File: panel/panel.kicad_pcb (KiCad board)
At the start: 2 copper layers, 199.5 x 80 mm, 381 parts, among them J1 Conn_01x02, J2 Conn_01x03, J3 Conn_01x05, J4 HRO-TYPE-C-31-M-12, J5 ICSP, SW1 SW_RESET, U1 CH340G, U2 ATmega328P-AU, U3 LM324DT, U4 LM324DT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

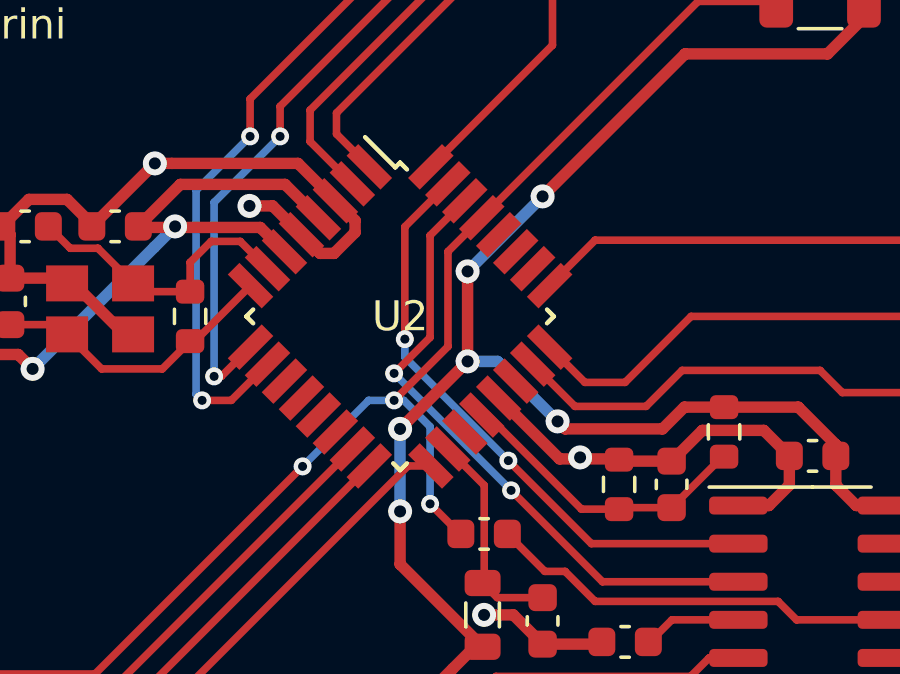
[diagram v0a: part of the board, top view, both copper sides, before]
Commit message: errata 1: rx and tx are flipped
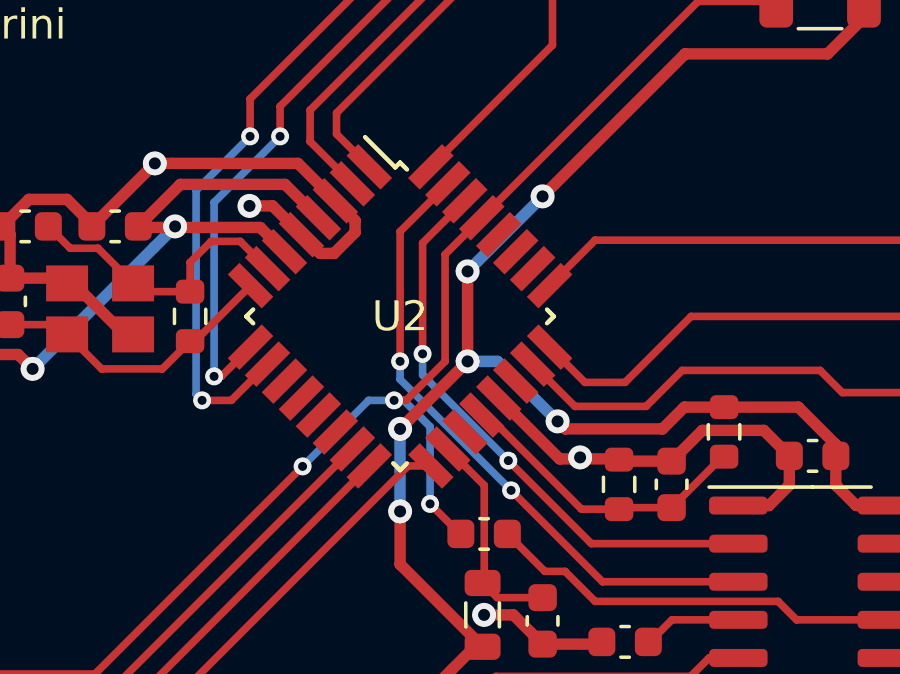
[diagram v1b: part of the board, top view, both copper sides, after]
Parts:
- removed the REF** at (239.0, 120.0) (x2)
- removed the REF** at (197.3, 120.6) (x2)
- removed the REF** at (61.7, 120.0) (x2)
- removed the REF** at (60.5, 118.9) (x2)
- removed the REF** at (61.1, 119.4) (x2)
- removed the REF** at (58.8, 117.1) (x2)
- removed the REF** at (59.4, 117.7) (x2)
- removed the REF** at (60.0, 118.3) (x2)
- removed the REF** at (60.0, 74.8) (x2)
- removed the REF** at (106.3, 117.7) (x2)
- removed the REF** at (193.8, 117.1) (x2)
- removed the REF** at (62.3, 72.5) (x2)
- removed the REF** at (59.4, 75.4) (x2)
- removed the REF** at (106.9, 117.1) (x2)
- removed the REF** at (61.7, 73.1) (x2)
- removed the REF** at (105.2, 118.9) (x2)
- removed the REF** at (105.7, 118.3) (x2)
- removed the REF** at (58.8, 76.0) (x2)
- removed the REF** at (61.1, 73.7) (x2)
- removed the REF** at (60.5, 74.2) (x2)
- removed the REF** at (103.4, 120.6) (x2)
- removed the REF** at (196.7, 120.0) (x2)
- removed the REF** at (104.6, 73.7) (x2)
- removed the REF** at (106.9, 76.0) (x2)
- removed the REF** at (106.3, 75.4) (x2)
- removed the REF** at (105.2, 74.2) (x2)
- removed the REF** at (103.4, 72.5) (x2)
- removed the REF** at (104.0, 73.1) (x2)
- removed the REF** at (105.7, 74.8) (x2)
- removed the REF** at (195.0, 118.3) (x2)
- removed the REF** at (194.4, 117.7) (x2)
- removed the REF** at (195.5, 118.9) (x2)
- removed the REF** at (196.1, 119.4) (x2)
- removed the REF** at (239.6, 119.4) (x2)
- removed the REF** at (195.0, 74.8) (x2)
- removed the REF** at (241.3, 117.7) (x2)
- removed the REF** at (197.3, 72.5) (x2)
- removed the REF** at (194.4, 75.4) (x2)
- removed the REF** at (241.9, 117.1) (x2)
- removed the REF** at (196.7, 73.1) (x2)
- removed the REF** at (238.4, 120.6) (x2)
- removed the REF** at (240.2, 118.9) (x2)
- removed the REF** at (240.7, 118.3) (x2)
- removed the REF** at (193.8, 76.0) (x2)
- removed the REF** at (196.1, 73.7) (x2)
- removed the REF** at (195.5, 74.2) (x2)
- removed the REF** at (239.6, 73.7) (x2)
- removed the REF** at (241.9, 76.0) (x2)
- removed the REF** at (241.3, 75.4) (x2)
- removed the REF** at (240.2, 74.2) (x2)
- removed the REF** at (238.4, 72.5) (x2)
- removed the REF** at (239.0, 73.1) (x2)
- removed the REF** at (240.7, 74.8) (x2)
- removed the REF** at (104.0, 120.0) (x2)
- removed the REF** at (104.6, 119.4) (x2)
- removed the REF** at (62.3, 120.6) (x2)
- added REF** (x2): NPTH, NPTH, F.Cu at (239.0, 120.0)
- added REF** (x2): NPTH, NPTH, F.Cu at (197.3, 120.6)
- added REF** (x2): NPTH, NPTH, F.Cu at (61.7, 120.0)
- added REF** (x2): NPTH, NPTH, F.Cu at (60.5, 118.9)
- added REF** (x2): NPTH, NPTH, F.Cu at (61.1, 119.4)
- added REF** (x2): NPTH, NPTH, F.Cu at (58.8, 117.1)
- added REF** (x2): NPTH, NPTH, F.Cu at (59.4, 117.7)
- added REF** (x2): NPTH, NPTH, F.Cu at (60.0, 118.3)
- added REF** (x2): NPTH, NPTH, F.Cu at (60.0, 74.8)
- added REF** (x2): NPTH, NPTH, F.Cu at (106.3, 117.7)
- added REF** (x2): NPTH, NPTH, F.Cu at (193.8, 117.1)
- added REF** (x2): NPTH, NPTH, F.Cu at (62.3, 72.5)
- added REF** (x2): NPTH, NPTH, F.Cu at (59.4, 75.4)
- added REF** (x2): NPTH, NPTH, F.Cu at (106.9, 117.1)
- added REF** (x2): NPTH, NPTH, F.Cu at (61.7, 73.1)
- added REF** (x2): NPTH, NPTH, F.Cu at (105.2, 118.9)
- added REF** (x2): NPTH, NPTH, F.Cu at (105.7, 118.3)
- added REF** (x2): NPTH, NPTH, F.Cu at (58.8, 76.0)
- added REF** (x2): NPTH, NPTH, F.Cu at (61.1, 73.7)
- added REF** (x2): NPTH, NPTH, F.Cu at (60.5, 74.2)
- added REF** (x2): NPTH, NPTH, F.Cu at (103.4, 120.6)
- added REF** (x2): NPTH, NPTH, F.Cu at (196.7, 120.0)
- added REF** (x2): NPTH, NPTH, F.Cu at (104.6, 73.7)
- added REF** (x2): NPTH, NPTH, F.Cu at (106.9, 76.0)
- added REF** (x2): NPTH, NPTH, F.Cu at (106.3, 75.4)
- added REF** (x2): NPTH, NPTH, F.Cu at (105.2, 74.2)
- added REF** (x2): NPTH, NPTH, F.Cu at (103.4, 72.5)
- added REF** (x2): NPTH, NPTH, F.Cu at (104.0, 73.1)
- added REF** (x2): NPTH, NPTH, F.Cu at (105.7, 74.8)
- added REF** (x2): NPTH, NPTH, F.Cu at (195.0, 118.3)
- added REF** (x2): NPTH, NPTH, F.Cu at (194.4, 117.7)
- added REF** (x2): NPTH, NPTH, F.Cu at (195.5, 118.9)
- added REF** (x2): NPTH, NPTH, F.Cu at (196.1, 119.4)
- added REF** (x2): NPTH, NPTH, F.Cu at (239.6, 119.4)
- added REF** (x2): NPTH, NPTH, F.Cu at (195.0, 74.8)
- added REF** (x2): NPTH, NPTH, F.Cu at (241.3, 117.7)
- added REF** (x2): NPTH, NPTH, F.Cu at (197.3, 72.5)
- added REF** (x2): NPTH, NPTH, F.Cu at (194.4, 75.4)
- added REF** (x2): NPTH, NPTH, F.Cu at (241.9, 117.1)
- added REF** (x2): NPTH, NPTH, F.Cu at (196.7, 73.1)
- added REF** (x2): NPTH, NPTH, F.Cu at (238.4, 120.6)
- added REF** (x2): NPTH, NPTH, F.Cu at (240.2, 118.9)
- added REF** (x2): NPTH, NPTH, F.Cu at (240.7, 118.3)
- added REF** (x2): NPTH, NPTH, F.Cu at (193.8, 76.0)
- added REF** (x2): NPTH, NPTH, F.Cu at (196.1, 73.7)
- added REF** (x2): NPTH, NPTH, F.Cu at (195.5, 74.2)
- added REF** (x2): NPTH, NPTH, F.Cu at (239.6, 73.7)
- added REF** (x2): NPTH, NPTH, F.Cu at (241.9, 76.0)
- added REF** (x2): NPTH, NPTH, F.Cu at (241.3, 75.4)
- added REF** (x2): NPTH, NPTH, F.Cu at (240.2, 74.2)
- added REF** (x2): NPTH, NPTH, F.Cu at (238.4, 72.5)
- added REF** (x2): NPTH, NPTH, F.Cu at (239.0, 73.1)
- added REF** (x2): NPTH, NPTH, F.Cu at (240.7, 74.8)
- added REF** (x2): NPTH, NPTH, F.Cu at (104.0, 120.0)
- added REF** (x2): NPTH, NPTH, F.Cu at (104.6, 119.4)
- added REF** (x2): NPTH, NPTH, F.Cu at (62.3, 120.6)
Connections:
- U2 pad 30: RX -> TX
- U2 pad 31: TX -> RX
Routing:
- net TX: track 20.1 -> 19.2 mm

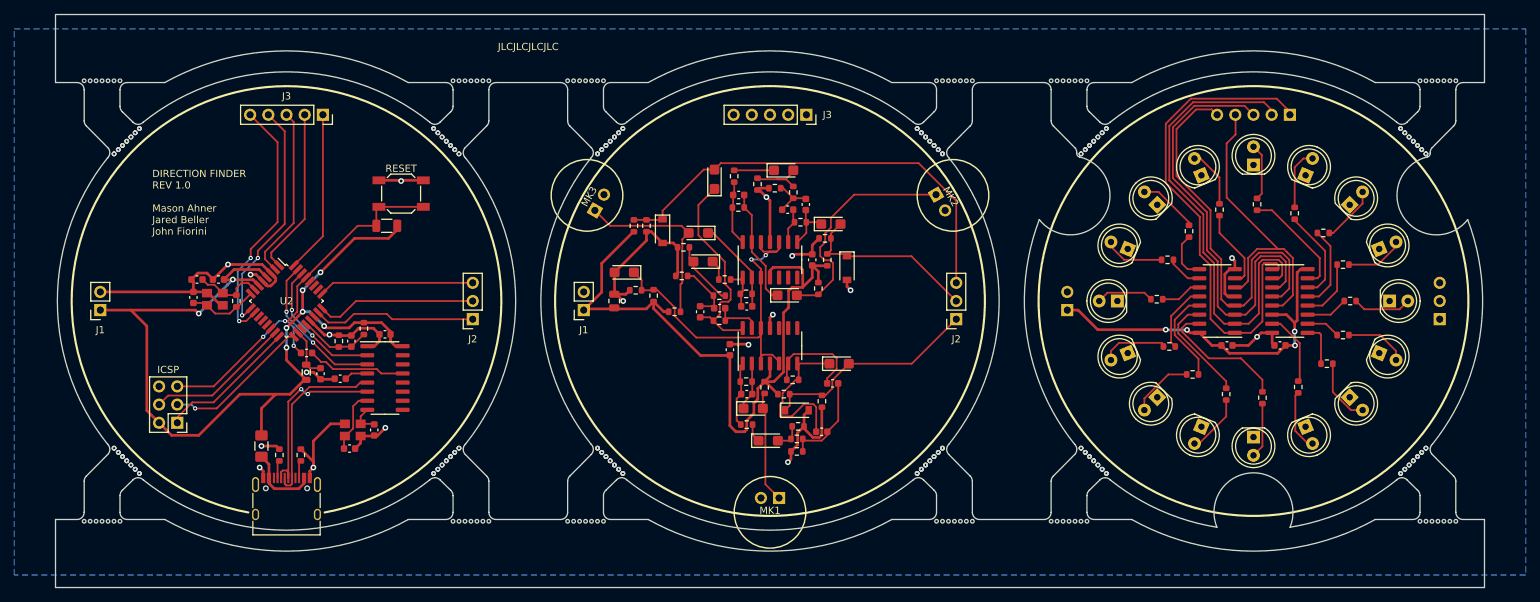
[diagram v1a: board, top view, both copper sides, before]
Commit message: errata 2: fix footprints
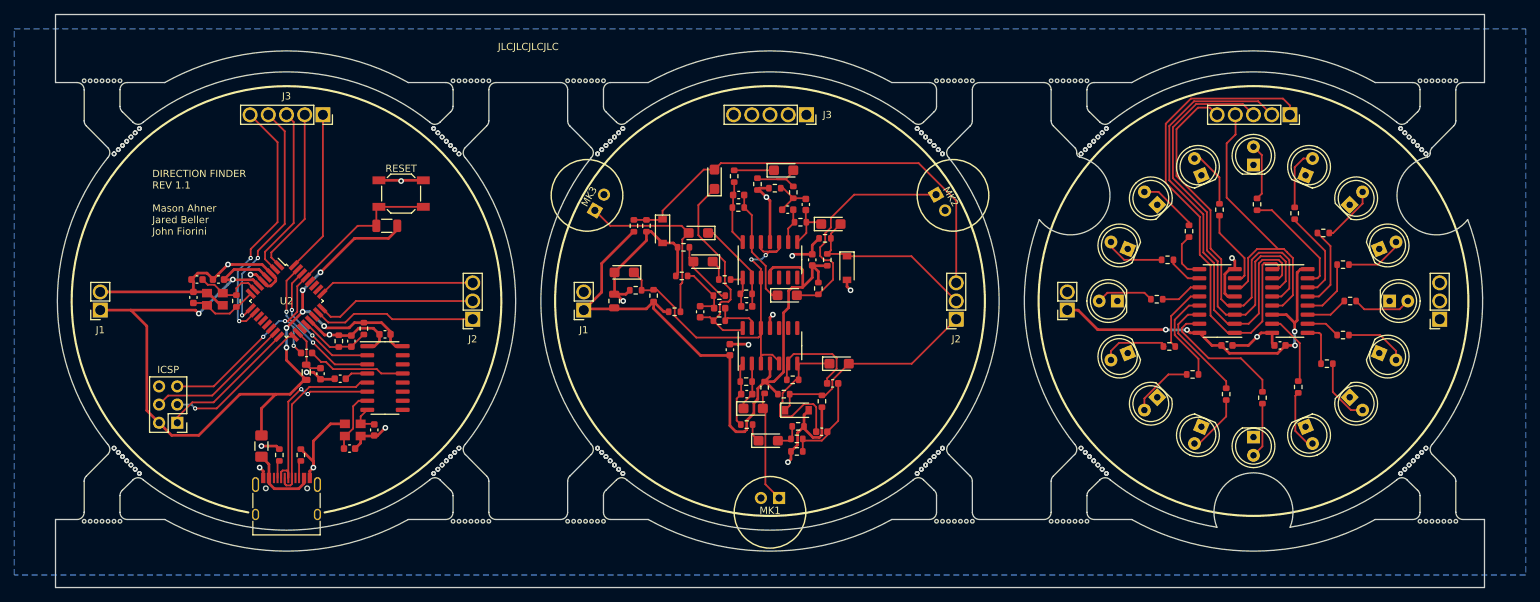
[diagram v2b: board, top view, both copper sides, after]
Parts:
- removed the REF** at (239.0, 120.0) (x2)
- removed the REF** at (197.3, 120.6) (x2)
- removed the REF** at (61.7, 120.0) (x2)
- removed the REF** at (60.5, 118.9) (x2)
- removed the REF** at (61.1, 119.4) (x2)
- removed the REF** at (58.8, 117.1) (x2)
- removed the REF** at (59.4, 117.7) (x2)
- removed the REF** at (60.0, 118.3) (x2)
- removed the REF** at (60.0, 74.8) (x2)
- removed the REF** at (106.3, 117.7) (x2)
- removed the REF** at (193.8, 117.1) (x2)
- removed the REF** at (62.3, 72.5) (x2)
- removed the REF** at (59.4, 75.4) (x2)
- removed the REF** at (106.9, 117.1) (x2)
- removed the REF** at (61.7, 73.1) (x2)
- removed the REF** at (105.2, 118.9) (x2)
- removed the REF** at (105.7, 118.3) (x2)
- removed the REF** at (58.8, 76.0) (x2)
- removed the REF** at (61.1, 73.7) (x2)
- removed the REF** at (60.5, 74.2) (x2)
- removed the REF** at (103.4, 120.6) (x2)
- removed the REF** at (196.7, 120.0) (x2)
- removed the REF** at (104.6, 73.7) (x2)
- removed the REF** at (106.9, 76.0) (x2)
- removed the REF** at (106.3, 75.4) (x2)
- removed the REF** at (105.2, 74.2) (x2)
- removed the REF** at (103.4, 72.5) (x2)
- removed the REF** at (104.0, 73.1) (x2)
- removed the REF** at (105.7, 74.8) (x2)
- removed the REF** at (195.0, 118.3) (x2)
- removed the REF** at (194.4, 117.7) (x2)
- removed the REF** at (195.5, 118.9) (x2)
- removed the REF** at (196.1, 119.4) (x2)
- removed the REF** at (239.6, 119.4) (x2)
- removed the REF** at (195.0, 74.8) (x2)
- removed the REF** at (241.3, 117.7) (x2)
- removed the REF** at (197.3, 72.5) (x2)
- removed the REF** at (194.4, 75.4) (x2)
- removed the REF** at (241.9, 117.1) (x2)
- removed the REF** at (196.7, 73.1) (x2)
- removed the REF** at (238.4, 120.6) (x2)
- removed the REF** at (240.2, 118.9) (x2)
- removed the REF** at (240.7, 118.3) (x2)
- removed the REF** at (193.8, 76.0) (x2)
- removed the REF** at (196.1, 73.7) (x2)
- removed the REF** at (195.5, 74.2) (x2)
- removed the REF** at (239.6, 73.7) (x2)
- removed the REF** at (241.9, 76.0) (x2)
- removed the REF** at (241.3, 75.4) (x2)
- removed the REF** at (240.2, 74.2) (x2)
- removed the REF** at (238.4, 72.5) (x2)
- removed the REF** at (239.0, 73.1) (x2)
- removed the REF** at (240.7, 74.8) (x2)
- removed the REF** at (104.0, 120.0) (x2)
- removed the REF** at (104.6, 119.4) (x2)
- removed the REF** at (62.3, 120.6) (x2)
- added REF** (x2): NPTH, NPTH, F.Cu at (239.0, 120.0)
- added REF** (x2): NPTH, NPTH, F.Cu at (197.3, 120.6)
- added REF** (x2): NPTH, NPTH, F.Cu at (61.7, 120.0)
- added REF** (x2): NPTH, NPTH, F.Cu at (60.5, 118.9)
- added REF** (x2): NPTH, NPTH, F.Cu at (61.1, 119.4)
- added REF** (x2): NPTH, NPTH, F.Cu at (58.8, 117.1)
- added REF** (x2): NPTH, NPTH, F.Cu at (59.4, 117.7)
- added REF** (x2): NPTH, NPTH, F.Cu at (60.0, 118.3)
- added REF** (x2): NPTH, NPTH, F.Cu at (60.0, 74.8)
- added REF** (x2): NPTH, NPTH, F.Cu at (106.3, 117.7)
- added REF** (x2): NPTH, NPTH, F.Cu at (193.8, 117.1)
- added REF** (x2): NPTH, NPTH, F.Cu at (62.3, 72.5)
- added REF** (x2): NPTH, NPTH, F.Cu at (59.4, 75.4)
- added REF** (x2): NPTH, NPTH, F.Cu at (106.9, 117.1)
- added REF** (x2): NPTH, NPTH, F.Cu at (61.7, 73.1)
- added REF** (x2): NPTH, NPTH, F.Cu at (105.2, 118.9)
- added REF** (x2): NPTH, NPTH, F.Cu at (105.7, 118.3)
- added REF** (x2): NPTH, NPTH, F.Cu at (58.8, 76.0)
- added REF** (x2): NPTH, NPTH, F.Cu at (61.1, 73.7)
- added REF** (x2): NPTH, NPTH, F.Cu at (60.5, 74.2)
- added REF** (x2): NPTH, NPTH, F.Cu at (103.4, 120.6)
- added REF** (x2): NPTH, NPTH, F.Cu at (196.7, 120.0)
- added REF** (x2): NPTH, NPTH, F.Cu at (104.6, 73.7)
- added REF** (x2): NPTH, NPTH, F.Cu at (106.9, 76.0)
- added REF** (x2): NPTH, NPTH, F.Cu at (106.3, 75.4)
- added REF** (x2): NPTH, NPTH, F.Cu at (105.2, 74.2)
- added REF** (x2): NPTH, NPTH, F.Cu at (103.4, 72.5)
- added REF** (x2): NPTH, NPTH, F.Cu at (104.0, 73.1)
- added REF** (x2): NPTH, NPTH, F.Cu at (105.7, 74.8)
- added REF** (x2): NPTH, NPTH, F.Cu at (195.0, 118.3)
- added REF** (x2): NPTH, NPTH, F.Cu at (194.4, 117.7)
- added REF** (x2): NPTH, NPTH, F.Cu at (195.5, 118.9)
- added REF** (x2): NPTH, NPTH, F.Cu at (196.1, 119.4)
- added REF** (x2): NPTH, NPTH, F.Cu at (239.6, 119.4)
- added REF** (x2): NPTH, NPTH, F.Cu at (195.0, 74.8)
- added REF** (x2): NPTH, NPTH, F.Cu at (241.3, 117.7)
- added REF** (x2): NPTH, NPTH, F.Cu at (197.3, 72.5)
- added REF** (x2): NPTH, NPTH, F.Cu at (194.4, 75.4)
- added REF** (x2): NPTH, NPTH, F.Cu at (241.9, 117.1)
- added REF** (x2): NPTH, NPTH, F.Cu at (196.7, 73.1)
- added REF** (x2): NPTH, NPTH, F.Cu at (238.4, 120.6)
- added REF** (x2): NPTH, NPTH, F.Cu at (240.2, 118.9)
- added REF** (x2): NPTH, NPTH, F.Cu at (240.7, 118.3)
- added REF** (x2): NPTH, NPTH, F.Cu at (193.8, 76.0)
- added REF** (x2): NPTH, NPTH, F.Cu at (196.1, 73.7)
- added REF** (x2): NPTH, NPTH, F.Cu at (195.5, 74.2)
- added REF** (x2): NPTH, NPTH, F.Cu at (239.6, 73.7)
- added REF** (x2): NPTH, NPTH, F.Cu at (241.9, 76.0)
- added REF** (x2): NPTH, NPTH, F.Cu at (241.3, 75.4)
- added REF** (x2): NPTH, NPTH, F.Cu at (240.2, 74.2)
- added REF** (x2): NPTH, NPTH, F.Cu at (238.4, 72.5)
- added REF** (x2): NPTH, NPTH, F.Cu at (239.0, 73.1)
- added REF** (x2): NPTH, NPTH, F.Cu at (240.7, 74.8)
- added REF** (x2): NPTH, NPTH, F.Cu at (104.0, 120.0)
- added REF** (x2): NPTH, NPTH, F.Cu at (104.6, 119.4)
- added REF** (x2): NPTH, NPTH, F.Cu at (62.3, 120.6)
- J1 (x3): footprint Connector_PinSocket_2.54mm:PinSocket_1x02_P2.54mm_Vertical -> df-parts:310-XX-102-41-001000
- J2 (x3): footprint Connector_PinSocket_2.54mm:PinSocket_1x03_P2.54mm_Vertical -> df-parts:310-XX-103-41-001000
- J3 (x3): footprint Connector_PinSocket_2.54mm:PinSocket_1x05_P2.54mm_Vertical -> df-parts:310-XX-105-41-001000
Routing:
- net D1: track 89.6 -> 89.0 mm
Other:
- board text added: "DIRECTION FINDER REV 1.1 Mason Ahner Jared Beller John Fiorini"
- board text removed: "DIRECTION FINDER REV 1.0 Mason Ahner Jared Beller John Fiorini"
